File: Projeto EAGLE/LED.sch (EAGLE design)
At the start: 8 parts, among them J1 CONECTOR_MACHO, J2 CONECTOR_FEMEA, Q1 BC817, U1 74HC132

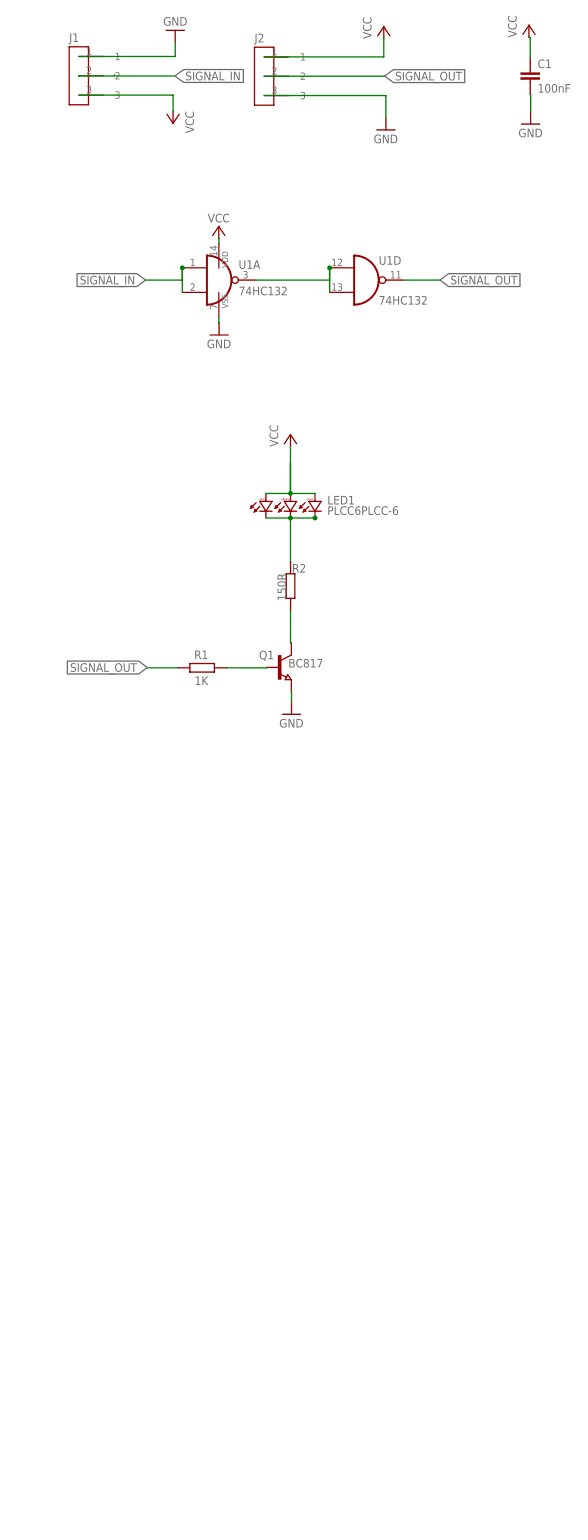
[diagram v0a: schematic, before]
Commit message: correção de pads, adição de label para versionamento e plano de VCC
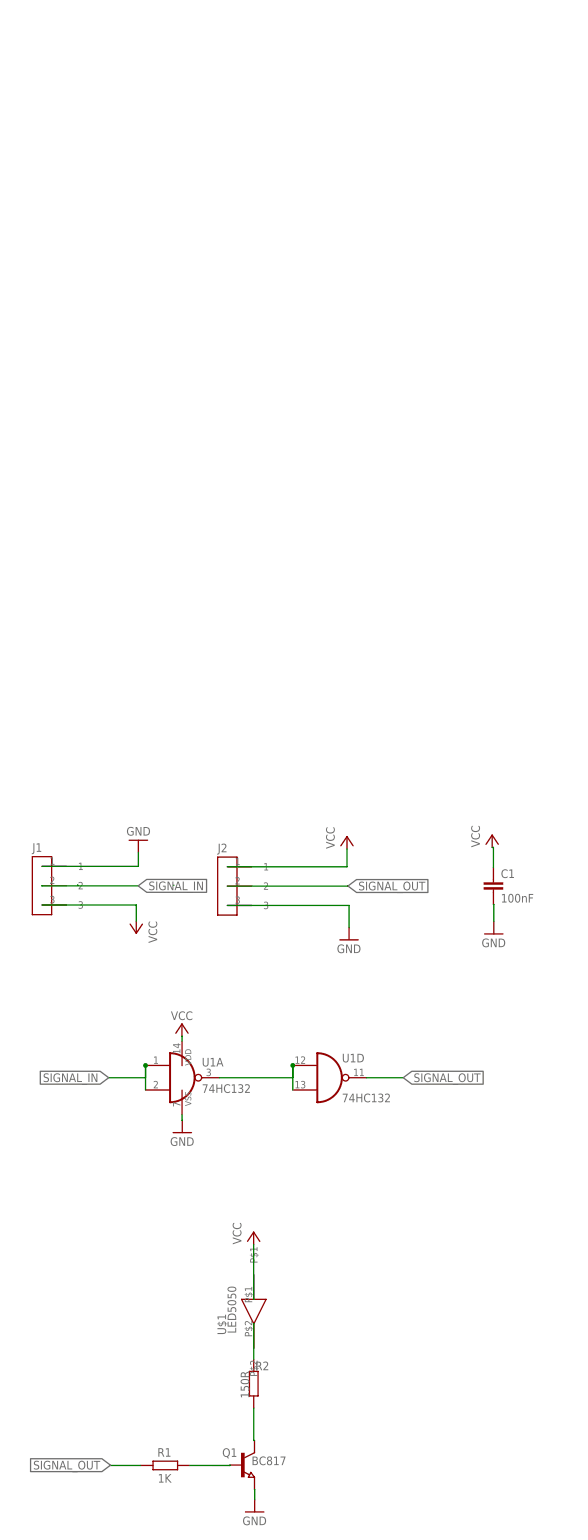
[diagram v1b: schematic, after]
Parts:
- removed LED1: PLCC6PLCC-6, PLCC-6-LED:PLCC6PLCC-6
- added U$1: LED5050, Eletroblocks Lib:LED5050
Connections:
- removed net N$5: LED1.BC, LED1.GC, LED1.RC, R2.2
- new net LED: R2.2, U$1.P$2
- net VCC: now also U$1.P$1; no longer LED1.BA, LED1.GA, LED1.RA
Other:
- moved on the sheet: C1, J1, J2, Q1, R1, R2, U1A, U1D
